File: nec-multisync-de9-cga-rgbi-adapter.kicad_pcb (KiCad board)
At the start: 2 copper layers, 52.1 x 36.1 mm, 8 parts, among them J1 DE9_Plug, J2 DE15_Receptacle_HighDensity, J3 DIN-8

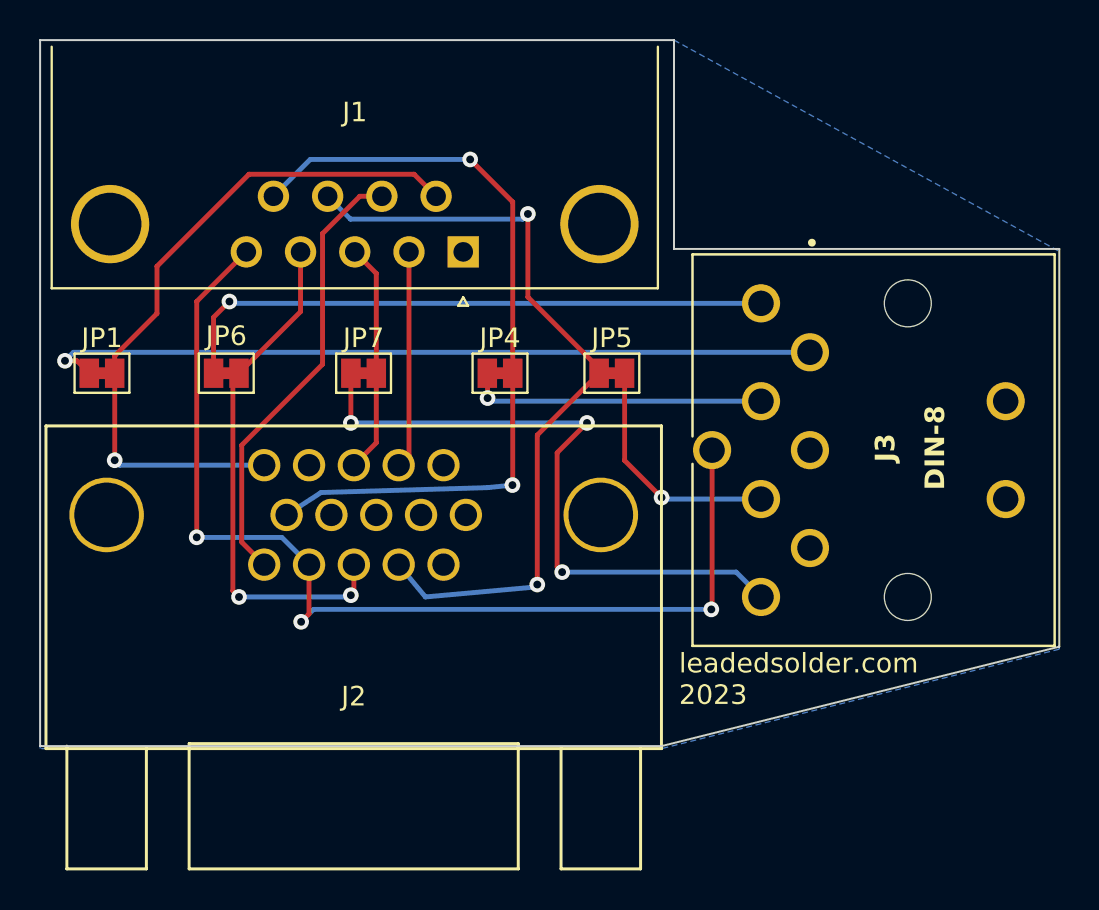
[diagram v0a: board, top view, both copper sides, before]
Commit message: Maybe reverse my bonehead fuckup of feeding 12V to the MultiSync's signal input
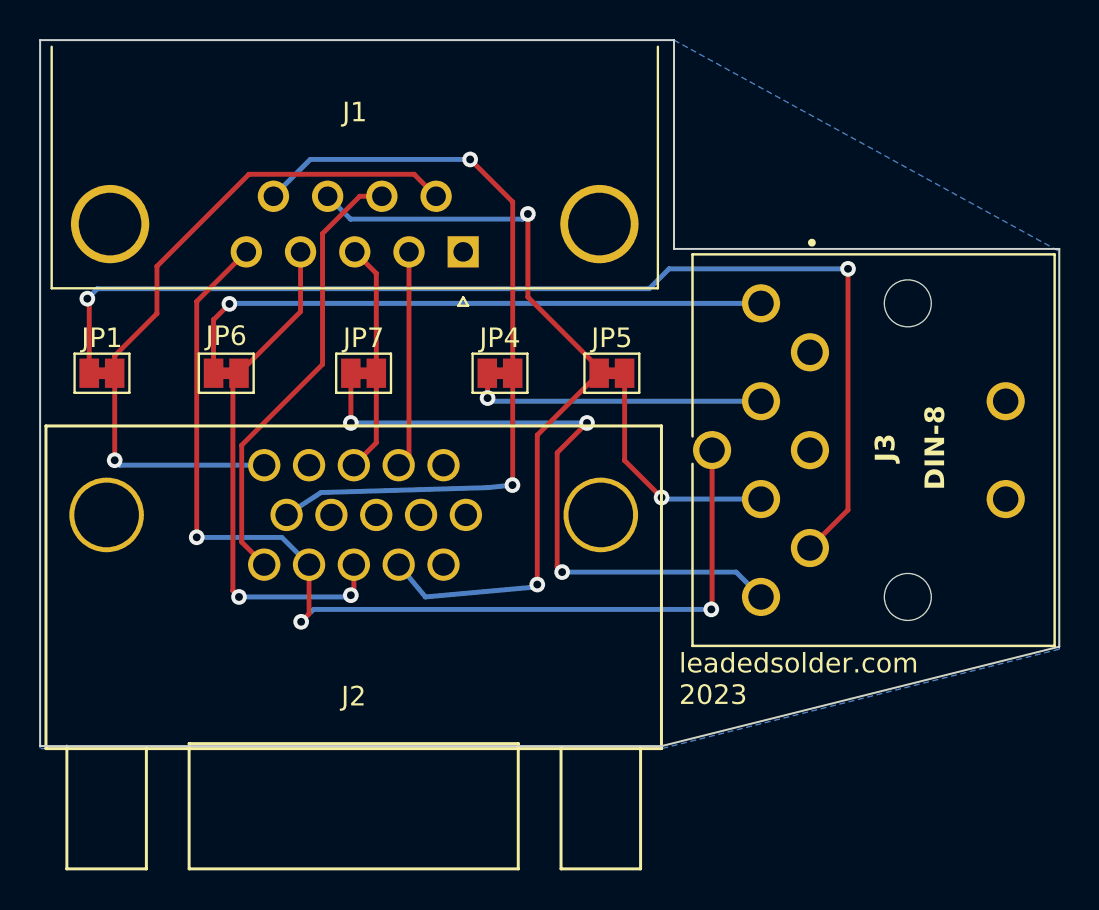
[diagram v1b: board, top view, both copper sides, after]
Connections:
- J3 pad 1: Net-(JP1-A) -> unconnected-(J3-Pad1)
- J3 pad 3: unconnected-(J3-Pad3) -> Net-(JP1-A)
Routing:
- net Net-(JP1-A): track 39.7 -> 58.4 mm, vias 1 -> 2
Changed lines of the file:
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@@
   (net 16 "Net-(JP7-A)")
   (net 17 "Net-(JP6-B)")
-  (net 18 "unconnected-(J3-Pad3)")
+  (net 18 "unconnected-(J3-Pad1)")
   (net 19 "Net-(JP4-A)")
   (net 20 "Net-(JP1-A)")
@@
     (pad "" np_thru_hole circle (at 7.5 5 90) (size 2.4 2.4) (drill 2.4) (layers "*.Cu" "*.Mask" "F.SilkS"))
     (pad "1" thru_hole circle (at 5 0 90) (size 1.95 1.95) (drill 1.3) (layers "*.Cu" "*.Mask")
-      (net 20 "Net-(JP1-A)") (pintype "passive"))
+      (net 18 "unconnected-(J3-Pad1)") (pintype "passive+no_connect"))
     (pad "2" thru_hole circle (at 0 0 90) (size 1.95 1.95) (drill 1.3) (layers "*.Cu" "*.Mask")
       (net 1 "GND") (pintype "passive"))
     (pad "3" thru_hole circle (at -5 0 90) (size 1.95 1.95) (drill 1.3) (layers "*.Cu" "*.Mask")
-      (net 18 "unconnected-(J3-Pad3)") (pintype "passive+no_connect"))
+      (net 20 "Net-(JP1-A)") (pintype "passive"))
     (pad "4" thru_hole circle (at 2.5 -2.5 90) (size 1.95 1.95) (drill 1.3) (layers "*.Cu" "*.Mask")
       (net 19 "Net-(JP4-A)") (pintype "passive"))
@@
   (segment (start 150.495 100.33) (end 141.605 100.33) (width 0.25) (layer "B.Cu") (net 16))
   (segment (start 142.875 92.71) (end 130.81 92.71) (width 0.25) (layer "B.Cu") (net 16))
-  (segment (start 123.795 87.318984) (end 124.606992 86.506992) (width 0.25) (layer "F.Cu") (net 17))
-  (segment (start 123.795 90.17) (end 123.795 87.318984) (width 0.25) (layer "F.Cu") (net 17))
-  (via (at 124.606992 86.506992) (size 0.8) (drill 0.4) (layers "F.Cu" "B.Cu") (net 17))
-  (segment (start 151.765 86.6) (end 124.7 86.6) (width 0.25) (layer "B.Cu") (net 17))
-  (segment (start 124.7 86.6) (end 124.606992 86.506992) (width 0.25) (layer "B.Cu") (net 17))
+  (segment (start 123.795 90.17) (end 123.795 87.438992) (width 0.25) (layer "F.Cu") (net 17))
+  (segment (start 123.795 87.438992) (end 124.606992 86.627) (width 0.25) (layer "F.Cu") (net 17))
+  (via (at 124.606992 86.627) (size 0.8) (drill 0.4) (layers "F.Cu" "B.Cu") (net 17))
+  (segment (start 151.765 86.6) (end 124.633992 86.6) (width 0.25) (layer "B.Cu") (net 17))
+  (segment (start 124.633992 86.6) (end 124.606992 86.627) (width 0.25) (layer "B.Cu") (net 17))
   (segment (start 137.795 91.44) (end 137.795 90.185) (width 0.25) (layer "F.Cu") (net 19))
   (segment (start 137.795 90.185) (end 137.78 90.17) (width 0.25) (layer "F.Cu") (net 19))
@@
   (segment (start 137.955 91.6) (end 137.795 91.44) (width 0.25) (layer "B.Cu") (net 19))
   (segment (start 151.765 91.6) (end 137.955 91.6) (width 0.25) (layer "B.Cu") (net 19))
-  (segment (start 116.205 89.535) (end 116.81 89.535) (width 0.25) (layer "F.Cu") (net 20))
-  (segment (start 116.81 89.535) (end 117.445 90.17) (width 0.25) (layer "F.Cu") (net 20))
-  (via (at 116.205 89.535) (size 0.8) (drill 0.4) (layers "F.Cu" "B.Cu") (net 20))
-  (segment (start 116.64 89.1) (end 116.205 89.535) (width 0.25) (layer "B.Cu") (net 20))
-  (segment (start 154.265 89.1) (end 116.64 89.1) (width 0.25) (layer "B.Cu") (net 20))
+  (segment (start 117.445 86.457) (end 117.445 90.17) (width 0.25) (layer "F.Cu") (net 20))
+  (segment (start 154.265 99.1) (end 156.21 97.155) (width 0.25) (layer "F.Cu") (net 20))
+  (segment (start 156.21 97.155) (end 156.21 84.836) (width 0.25) (layer "F.Cu") (net 20))
+  (segment (start 117.348 86.36) (end 117.445 86.457) (width 0.25) (layer "F.Cu") (net 20))
+  (via (at 156.21 84.836) (size 0.8) (drill 0.4) (layers "F.Cu" "B.Cu") (net 20))
+  (via (at 117.348 86.36) (size 0.8) (drill 0.4) (layers "F.Cu" "B.Cu") (net 20))
+  (segment (start 117.856 85.852) (end 117.348 86.36) (width 0.25) (layer "B.Cu") (net 20))
+  (segment (start 156.21 84.836) (end 147.066 84.836) (width 0.25) (layer "B.Cu") (net 20))
+  (segment (start 147.066 84.836) (end 146.05 85.852) (width 0.25) (layer "B.Cu") (net 20))
+  (segment (start 146.05 85.852) (end 117.856 85.852) (width 0.25) (layer "B.Cu") (net 20))
   (segment (start 146.685 96.52) (end 144.795 94.63) (width 0.25) (layer "F.Cu") (net 21))
   (segment (start 144.795 94.63) (end 144.795 90.17) (width 0.25) (layer "F.Cu") (net 21))

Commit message: Label nets
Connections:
- net Net-(JP1-A) renamed /P6_I
- net Net-(JP4-A) renamed /P6_Vs
- net Net-(JP5-B) renamed /P6_Hs
- net Net-(JP6-B) renamed /P6_G
- net Net-(JP7-A) renamed /P6_R

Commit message: Prepare to flip DIN
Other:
- board text added: "Hs"
- board text added: "Vs"
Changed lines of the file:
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@@
     (effects (font (size 1 1) (thickness 0.15)) (justify mirror))
+  )
+  (gr_text "Hs" (at 130.556 79.756) (layer "B.SilkS")
+    (effects (font (size 1 1) (thickness 0.15)) (justify left bottom mirror))
+  )
+  (gr_text "Vs" (at 127.762 79.756) (layer "B.SilkS")
+    (effects (font (size 1 1) (thickness 0.15)) (justify left bottom mirror))
   )
   (gr_text "male to ibm pc" (at 136.652 76.454) (layer "B.SilkS")

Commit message: World's ugliest reroute
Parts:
- moved JP5 25.0 mm to (119.1, 90.2)
- moved JP7 12.7 mm to (144.2, 90.2)
- moved JP3 7.29 mm to (125.4, 90.2)
- moved JP6 7.20 mm to (131.6, 90.2)
- moved JP4 0.53 mm to (137.9, 90.2)
- renumbered JP1 to JP3
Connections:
- net /P6_G renamed /P6_Red
- net /P6_R renamed /P6_Green
- J3 pad 3: /P6_I -> /P6_Intens
- J3 pad 4: /P6_Vs -> /P6_Hs
- J3 pad 5: /P6_Hs -> /P6_Vs
- JP3 pad 1: /P6_I -> /EGA_Green1_Intensity
- JP3 pad 2: /EGA_Green1_Intensity -> /P6_Intens
- JP4 pad 1: /P6_Vs -> /HSync
- JP4 pad 2: /VSync -> /P6_Hs
- JP5 pad 1: /HSync -> /VSync
- JP5 pad 2: /P6_Hs -> /P6_Vs
- JP6 pad 1: /EGA_Green0 -> /EGA_Red0
- JP7 pad 2: /EGA_Red0 -> /EGA_Green0
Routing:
- net /P6_I: track 58.4 -> 0.00 mm, vias 2 -> 0
- net /P6_Intens: track 0.00 -> 43.7 mm, vias 0 -> 2
- net /P6_Vs: track 15.3 -> 34.9 mm
- net /EGA_Green0: track 26.6 -> 42.6 mm, vias 2 -> 1
- net /VSync: track 40.3 -> 28.7 mm
- net /P6_Green: track 33.6 -> 22.2 mm, vias 3 -> 1
- net /EGA_Blue1: track 22.9 -> 33.9 mm
- net /HSync: track 40.5 -> 32.8 mm, vias 2 -> 0
- net /EGA_Green1_Intensity: track 35.2 -> 28.1 mm, vias 1 -> 2
- net /P6_Red: track 31.0 -> 24.4 mm
- net /EGA_Red0: track 11.8 -> 15.4 mm
- net /EGA_Blue0: track 54.4 -> 52.2 mm, vias 3 -> 0
- net /P6_Hs: track 12.2 -> 14.2 mm
